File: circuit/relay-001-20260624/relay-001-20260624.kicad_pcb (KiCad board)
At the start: 2 copper layers, 169 x 126.3 mm, 15 parts, among them J1 Dribbler_{Back}, J10 MD_{Power}, J11 Motor1, J12 Motor2, J13 Motor3, J14 Motor4, J15 Voltmeter, J2 Kicker-Board, J3 MD_{Signal}, J4 Main-Board, J5 Power_{5V}, J6 Power_{VCC}, J7 Power_{Logic}, J8 Line_{Power}, J9 Line_{UART}

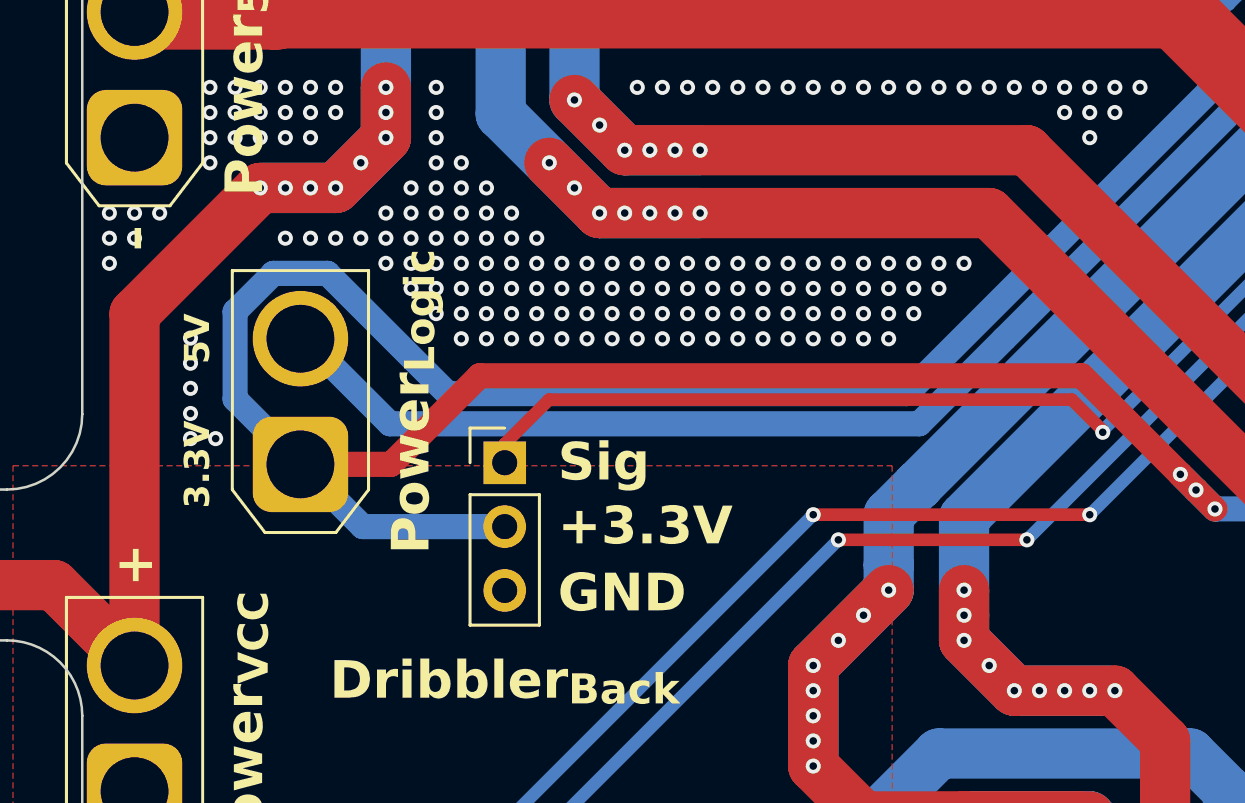
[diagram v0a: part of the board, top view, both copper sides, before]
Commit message: Update 供給基板のXT30の向きを変更、それに伴う電源基板の回路図も変更
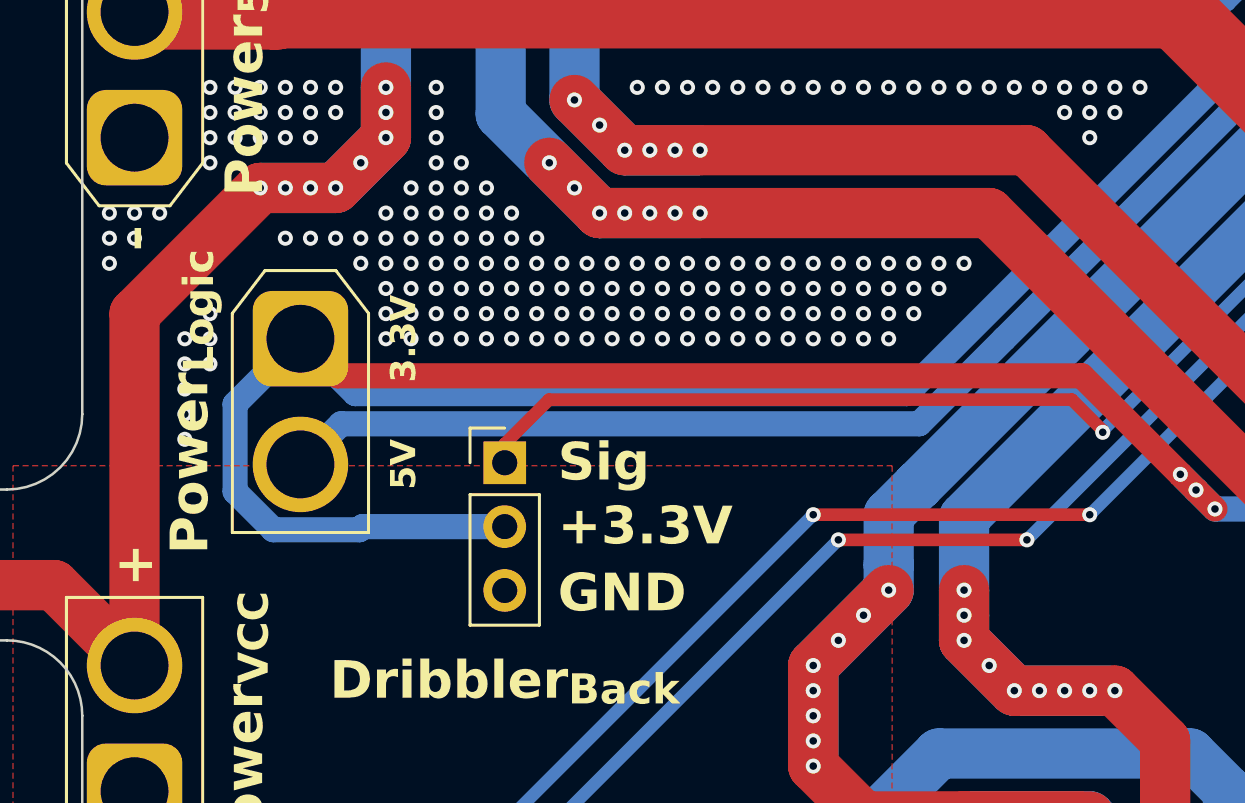
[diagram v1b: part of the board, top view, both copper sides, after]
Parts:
- moved J7 5.00 mm to (-28.4, -3.00), turned to -90 degrees
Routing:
- net +3.3V: track 208.8 -> 206.1 mm
- net +5V: track 88.4 -> 87.7 mm
- net GND: vias 1608 -> 1617
